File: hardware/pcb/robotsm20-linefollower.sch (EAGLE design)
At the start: 136 parts, among them Q5 BSS138LT3G, Q6 BSS138LT3G, Q7 BSS138LT3G, Q8 BSS138LT3G, U1 STM32F405RG

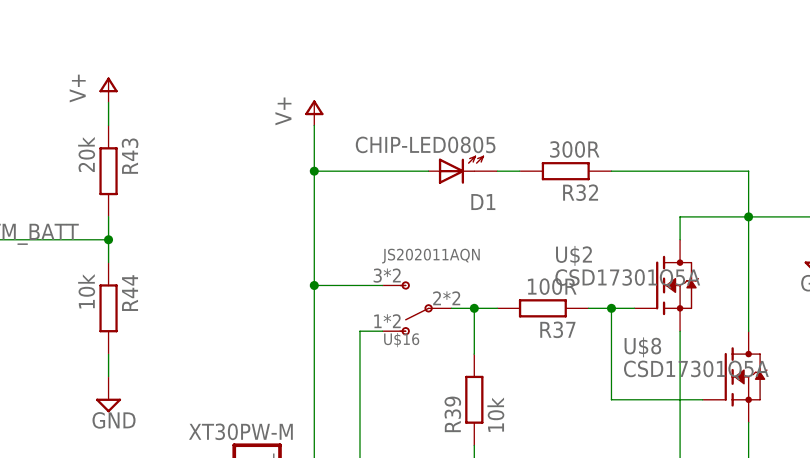
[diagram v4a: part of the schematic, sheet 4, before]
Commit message: Moved components in board
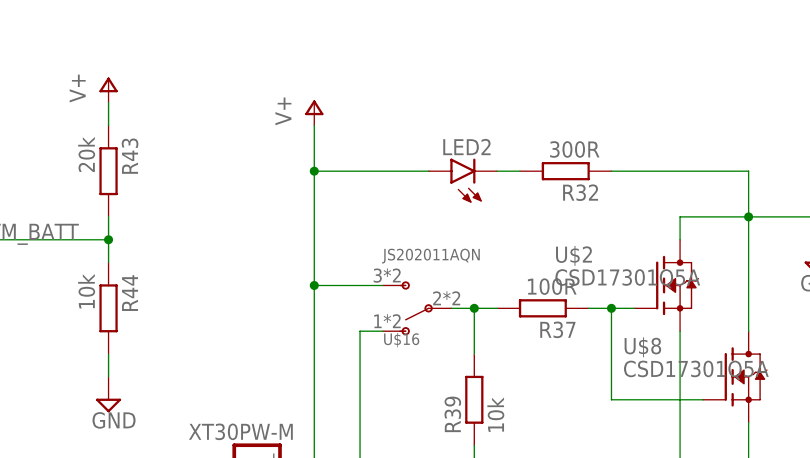
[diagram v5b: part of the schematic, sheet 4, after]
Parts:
- removed D1: CHIP-LED0805, CASE-LED:CHIP-LED0805
- added LED2: (no value), led:LEDCHIPLED_0603
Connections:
- net N$38: now also LED2.C; no longer D1.K
- net V+: now also LED2.A; no longer D1.A
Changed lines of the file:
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@@
 <part name="U$16" library="Switches" library_urn="urn:adsk.eagle:library:17810526" deviceset="JS202011AQN" device="" package3d_urn="urn:adsk.eagle:package:17810530/2"/>
 <part name="R37" library="rcl" library_urn="urn:adsk.eagle:library:334" deviceset="R-EU_" device="R0603" package3d_urn="urn:adsk.eagle:package:23555/3" value="100R"/>
-<part name="D1" library="CASE-LED" deviceset="CHIP-LED0805" device="" package3d_urn="urn:adsk.eagle:package:7889636/1"/>
 <part name="R32" library="rcl" library_urn="urn:adsk.eagle:library:334" deviceset="R-EU_" device="R0603" package3d_urn="urn:adsk.eagle:package:23555/3" value="300R"/>
 <part name="R35" library="rcl" library_urn="urn:adsk.eagle:library:334" deviceset="R-EU_" device="R0603" package3d_urn="urn:adsk.eagle:package:23555/3" value="10k"/>
@@
 <part name="U$5" library="Isaks Bibliotek" library_urn="urn:adsk.eagle:library:11889733" deviceset="DIODE_1N4148WX" device="" package3d_urn="urn:adsk.eagle:package:12971321/3"/>
 <part name="C47" library="rcl" library_urn="urn:adsk.eagle:library:334" deviceset="C-EU" device="C0805" package3d_urn="urn:adsk.eagle:package:23617/2"/>
-<part name="XLINE" library="CASE-JST" library_urn="urn:adsk.eagle:library:5637561" deviceset="ZR_B7B-ZR" device="" package3d_urn="urn:adsk.eagle:package:5644772/1" value="ZH"/>
+<part name="XLINE" library="CASE-JST" library_urn="urn:adsk.eagle:library:5637561" deviceset="ZR_B7B-ZR" device="" package3d_urn="urn:adsk.eagle:package:5644772/2" value="ZH"/>
 <part name="+3V13" library="supply1" library_urn="urn:adsk.eagle:library:371" deviceset="+3V3" device=""/>
 <part name="SUPPLY80" library="supply2" library_urn="urn:adsk.eagle:library:372" deviceset="GND" device=""/>
@@
 <part name="SUPPLY22" library="supply2" library_urn="urn:adsk.eagle:library:372" deviceset="GND" device=""/>
 <part name="RSENSE" library="rcl" library_urn="urn:adsk.eagle:library:334" deviceset="R-EU_" device="R2512W" package3d_urn="urn:adsk.eagle:package:23565/2" value="R002"/>
+<part name="LED2" library="led" library_urn="urn:adsk.eagle:library:259" deviceset="LED" device="CHIPLED_0603" package3d_urn="urn:adsk.eagle:package:15822/2"/>
 </parts>
 <sheets>
@@
 <attribute name="VALUE" x="168.91" y="102.362" size="1.778" layer="96" rot="R180"/>
 </instance>
-<instance part="D1" gate="G$1" x="154.94" y="114.3" smashed="yes" rot="R90" grouprefs="BATTERY">
-<attribute name="NAME" x="160.02" y="111.76" size="1.778" layer="95" rot="R180"/>
-<attribute name="VALUE" x="160.02" y="118.11" size="1.778" layer="96" rot="R180"/>
-</instance>
 <instance part="R32" gate="G$1" x="167.64" y="114.3" smashed="yes" rot="R180" grouprefs="BATTERY">
 <attribute name="NAME" x="171.45" y="112.8014" size="1.778" layer="95" rot="R180"/>
@@
 <attribute name="VALUE" x="54.102" y="46.99" size="1.778" layer="96" rot="R90"/>
 </instance>
+<instance part="LED2" gate="G$1" x="154.94" y="114.3" smashed="yes" rot="R90">
+<attribute name="NAME" x="159.512" y="117.856" size="1.778" layer="95" rot="R180"/>
+<attribute name="VALUE" x="159.512" y="120.015" size="1.778" layer="96" rot="R180"/>
+</instance>
 </instances>
 <busses>
@@
 <wire x1="147.32" y1="101.6" x2="139.7" y2="101.6" width="0.1524" layer="91" grouprefs="BATTERY"/>
 <junction x="139.7" y="101.6" grouprefs="BATTERY"/>
-<pinref part="D1" gate="G$1" pin="A"/>
 <wire x1="152.4" y1="114.3" x2="139.7" y2="114.3" width="0.1524" layer="91" grouprefs="BATTERY"/>
 <junction x="139.7" y="114.3" grouprefs="BATTERY"/>
+<pinref part="LED2" gate="G$1" pin="A"/>
 </segment>
 <segment>
@@
 <net name="N$38" class="0">
 <segment>
-<pinref part="D1" gate="G$1" pin="K"/>
 <pinref part="R32" gate="G$1" pin="2"/>
 <wire x1="160.02" y1="114.3" x2="162.56" y2="114.3" width="0.1524" layer="91" grouprefs="BATTERY"/>
+<pinref part="LED2" gate="G$1" pin="C"/>
 </segment>
 </net>

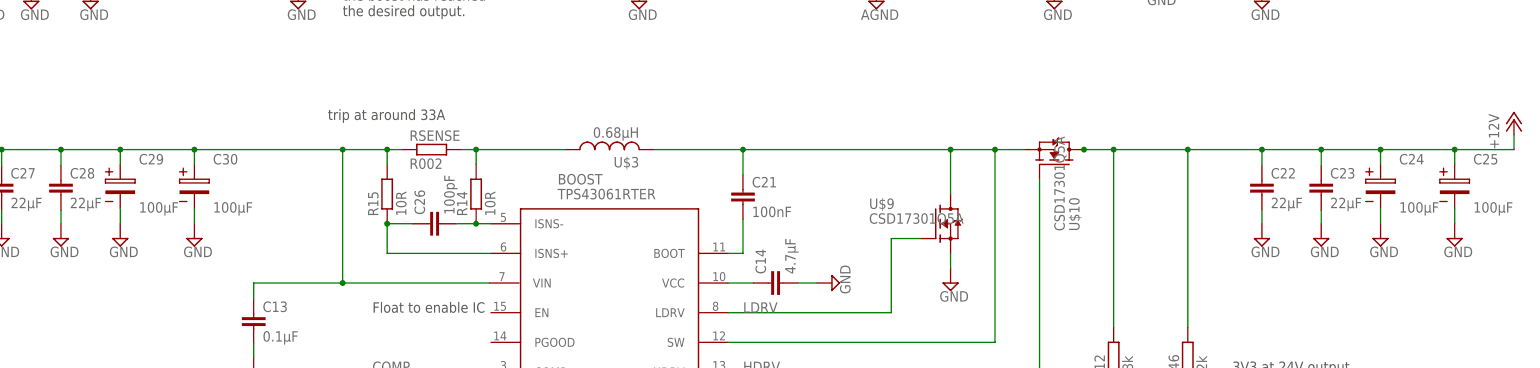
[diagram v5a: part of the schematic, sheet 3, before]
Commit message: 3D file update on components
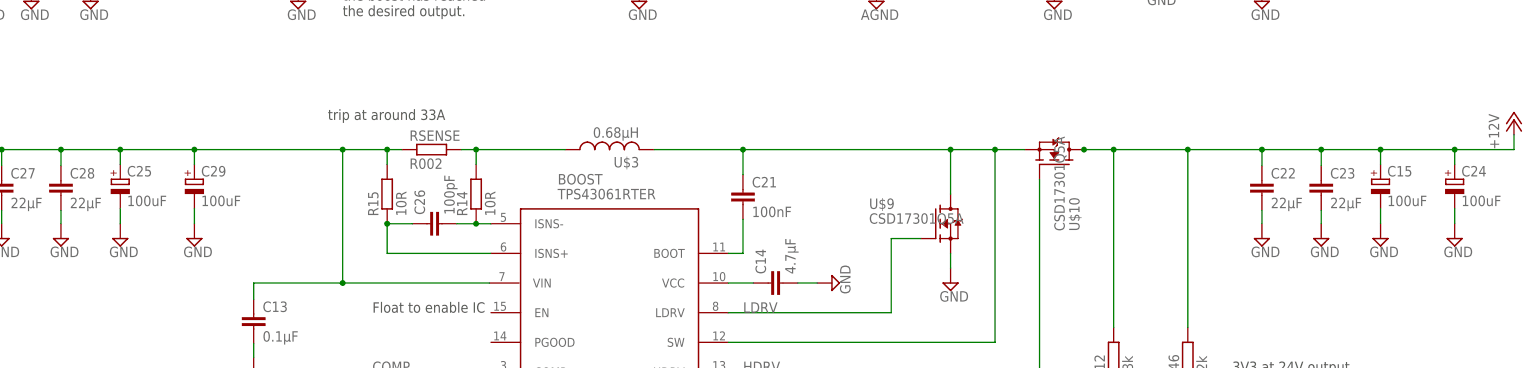
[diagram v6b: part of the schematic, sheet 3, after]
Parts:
- removed C5: 100µF, Passive:WCAP-ASLL_6,3X7,7_865060445005
- removed R33, R34: 10k, CASE-RCL:R0603
- added C15: 100uF, Passive:WCAP-ASLL-WEWCAP-ASLL
- added R13, R16: 10k, rcl:R-EU_R0603
- C24, C25, C29, C30, C4: value 100µF -> 100uF; device Passive:WCAP-ASLL_6,3X7,7_865060445005 -> Passive:WCAP-ASLL-WEWCAP-ASLL
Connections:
- net +12V: now also C15.+, C24.+; no longer C24.1, C25.1
- net 12V: now also C30.+, C4.+; no longer C4.1, C5.1
- net BOOT0: now also R13.2; no longer R34.2
- net BOOT1: now also R16.1; no longer R33.1
- net GND: now also C15.-, C24.-, C25.-, C29.-, C30.-, C4.-; no longer C24.2, C25.2, C29.2, C30.2, C4.2, C5.2
- net N$26: now also R16.2; no longer R33.2
- net N$34: now also R13.1; no longer R34.1
- net V+: now also C25.+, C29.+; no longer C29.1, C30.1

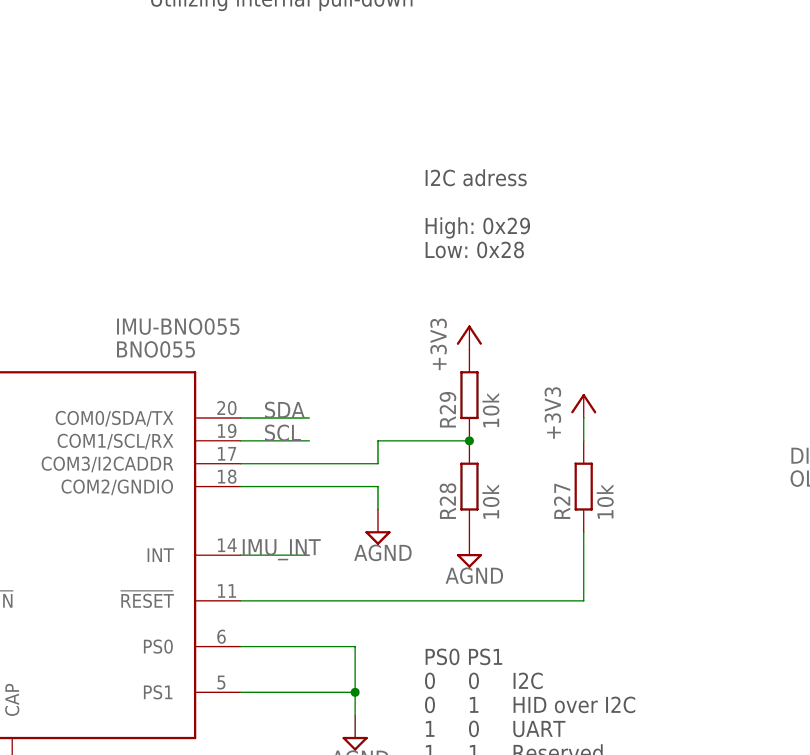
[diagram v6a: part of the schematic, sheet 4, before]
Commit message: Routed motor driver, boost
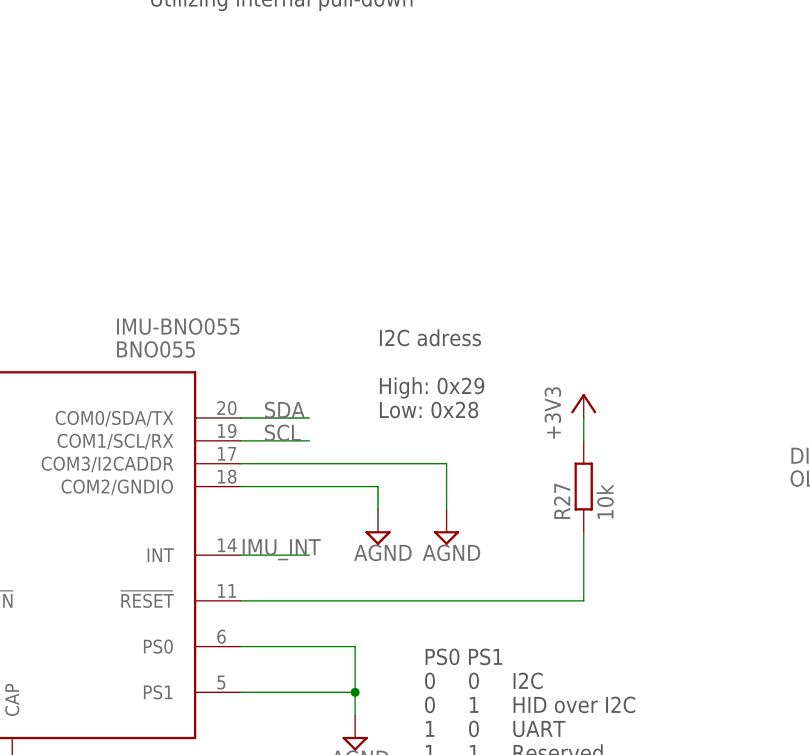
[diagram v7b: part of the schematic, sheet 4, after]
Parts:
- removed R28, R29: 10k, rcl:R-EU_R0603
- C31, C32, C33, C34, C35, C36, C37, C38, C39, C40, C42, C43, C44, C45, COSC, CVCC: device rcl:C-EUC0805 -> rcl:C-EUC0603
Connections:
- removed net 12V: C30.+, C4.+, C6.1, C7.1, MOTORDRIVER.VMA, MOTORDRIVER.VMB
- removed net N$39: IMU-BNO055.COM3/I2CADDR, R28.2, R29.1
- net +12V: now also C30.+, C4.+, C6.1, C7.1, MOTORDRIVER.VMA, MOTORDRIVER.VMB
- net +3V3: no longer R29.2
- net AGND: now also IMU-BNO055.COM3/I2CADDR; no longer R28.1

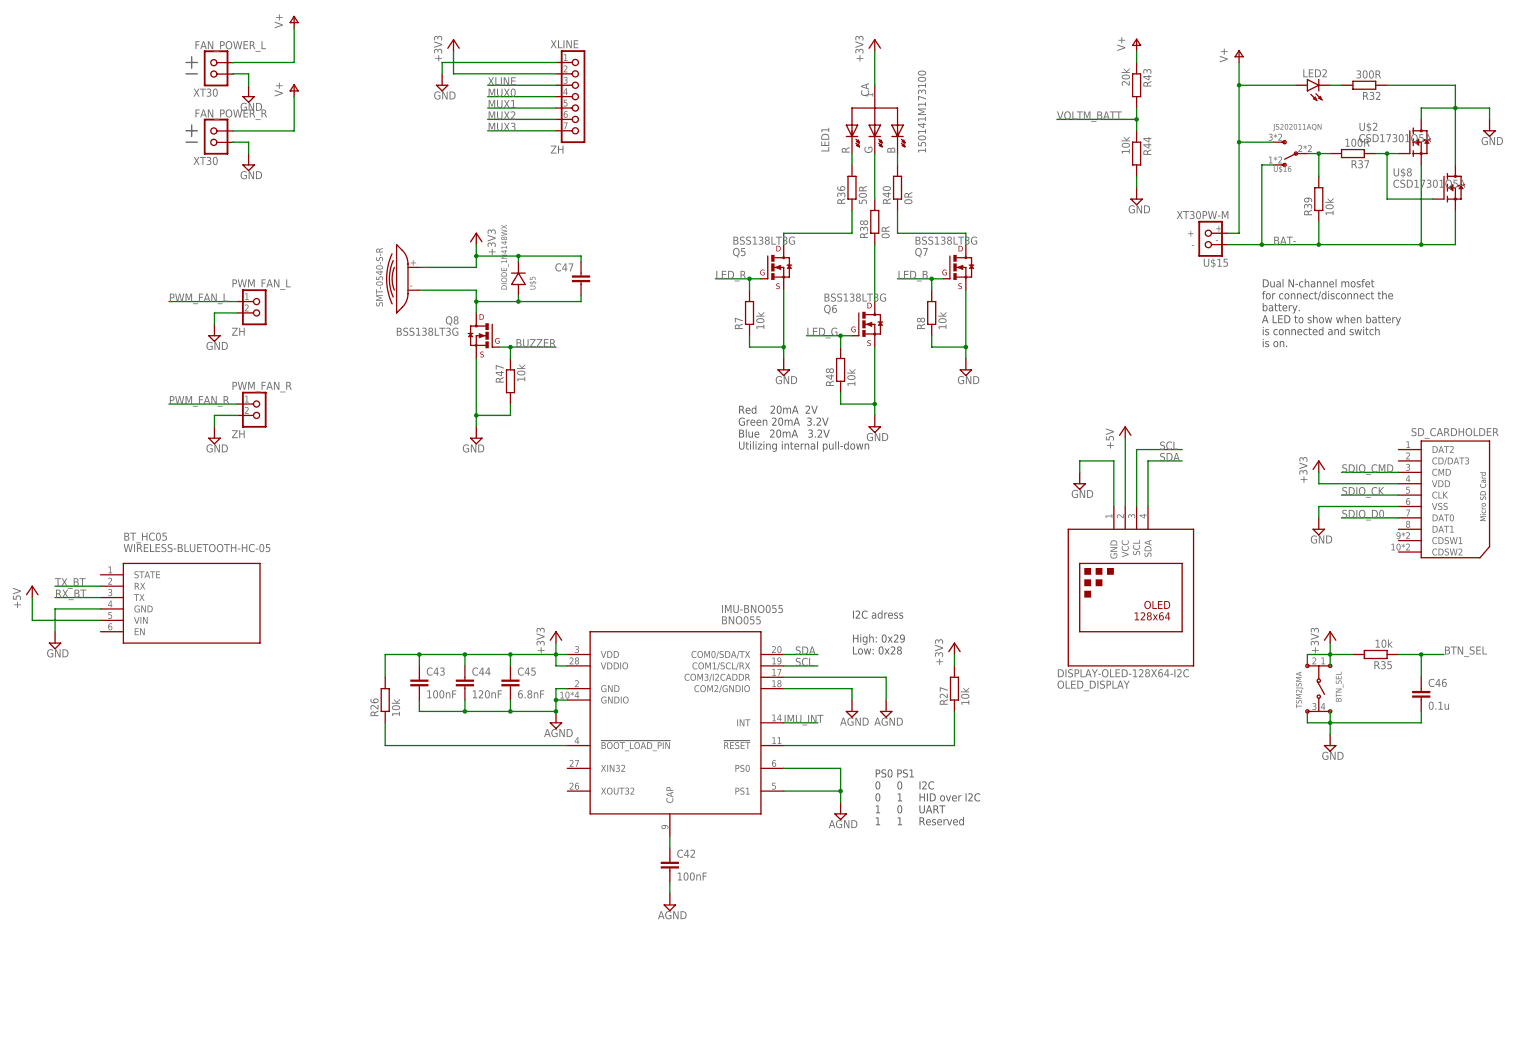
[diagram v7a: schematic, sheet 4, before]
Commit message: 3D packages update from components
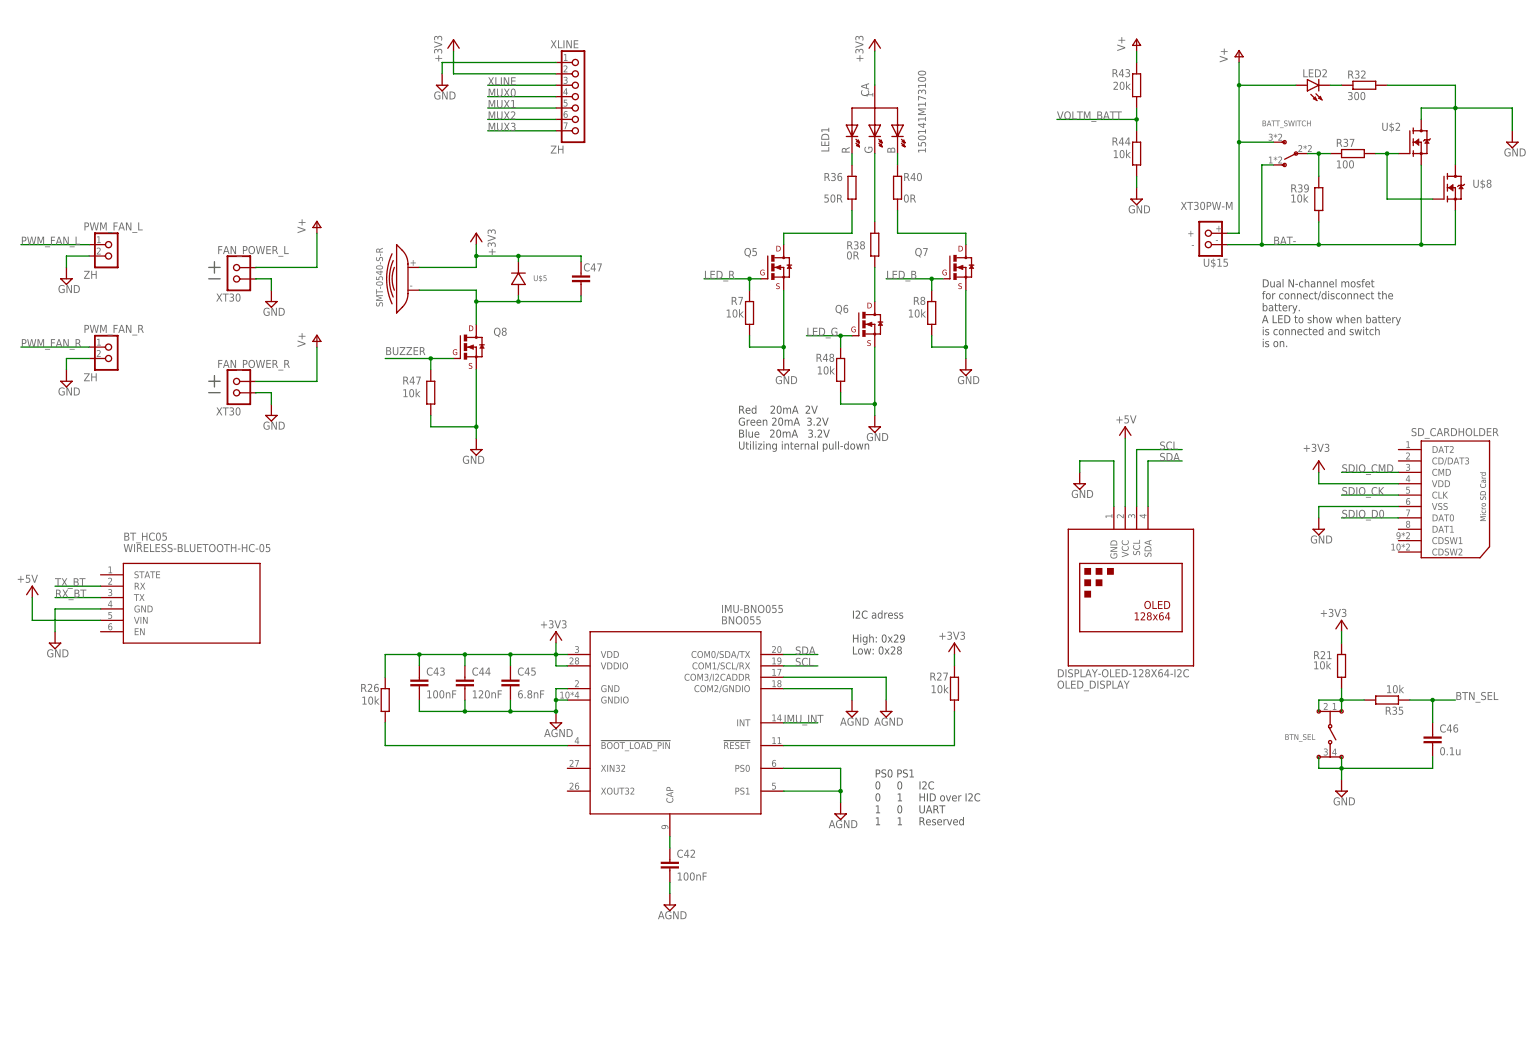
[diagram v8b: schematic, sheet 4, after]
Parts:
- removed TP1, TP2: TEST-POINT3X5, Isaks Bibliotek:TEST-POINT3X5
- added R21: 10k, rcl:R-EU_R0603
- added TP_12V, TP_1V8, TP_3V3, TP_5V, TP_LO1, TP_LO2: TEST-POINT3X5, Isaks Bibliotek:TEST-POINT3X5
- MOTOR_L, MOTOR_R: value EH-2 -> XH-02; device CASE-JST:EH_B2B-EH -> CASE-JST:XH-02
- R32: value 300R -> 300
- R37: value 100R -> 100
- renumbered BOOT to BOOT_SELECT, U$16 to BATT_SWITCH, U$4 to BTN_RESET
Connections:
- new net N$1: BTN_SEL.1, BTN_SEL.2, R21.2, R35.2
- net +12V: now also TP_12V.1
- net +3V3: now also R21.1, TP_3V3.1; no longer BTN_SEL.1, BTN_SEL.2, ENC_L.4, ENC_R.4, R35.2
- net +5V: now also ENC_L.4, ENC_R.4, TP_5V.1
- net AGND: now also C32.2, C33.2, U1.VSSA; no longer ENC_L.3, ENC_R.3
- net GND: now also ENC_L.3, ENC_R.3; no longer C32.2, C33.2, U1.VSSA
- net LO1: now also TP_LO1.1; no longer TP2.1
- net LO2: now also TP_LO2.1; no longer TP1.1
- net VREF: now also TP_1V8.1
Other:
- note added: "BOOT0=0 BOOT1=X - Main flash memory (your uploaded code) BOOT0=1 BOOT1=0 - System momory (internal serial USART1 boot loader) BOOT0=1 BOOT1=1 - Embedded SRAM Applies after reboot"
- note removed: "BOOT0=0 BOOT1=x - main flash memory (your uploaded code) BOOT0=1 BOOT1=0 - System momory (internal serial USART1 boot loader) BOOT0=1 BOOT1=1 - Embedded SRAM Applies after reboot"
- note removed: "Should be a filtered 3.3V Used for ADC"
- moved on the sheet: BTN_SEL, C46, FAN_POWER_L, FAN_POWER_R, MOTOR_L, MOTOR_R, PWM_FAN_L, PWM_FAN_R, Q8, R35, R38, R47
